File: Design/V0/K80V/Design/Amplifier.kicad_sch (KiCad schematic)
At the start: 51 parts, among them Q1 BC850, U1 AD8012, U2 AD8012, U3 LM4050AEM3-2.5+T, U4 OPA828, U5 INA828, U6 AD5752AREZ, U7 ADA4807, U8 X9118

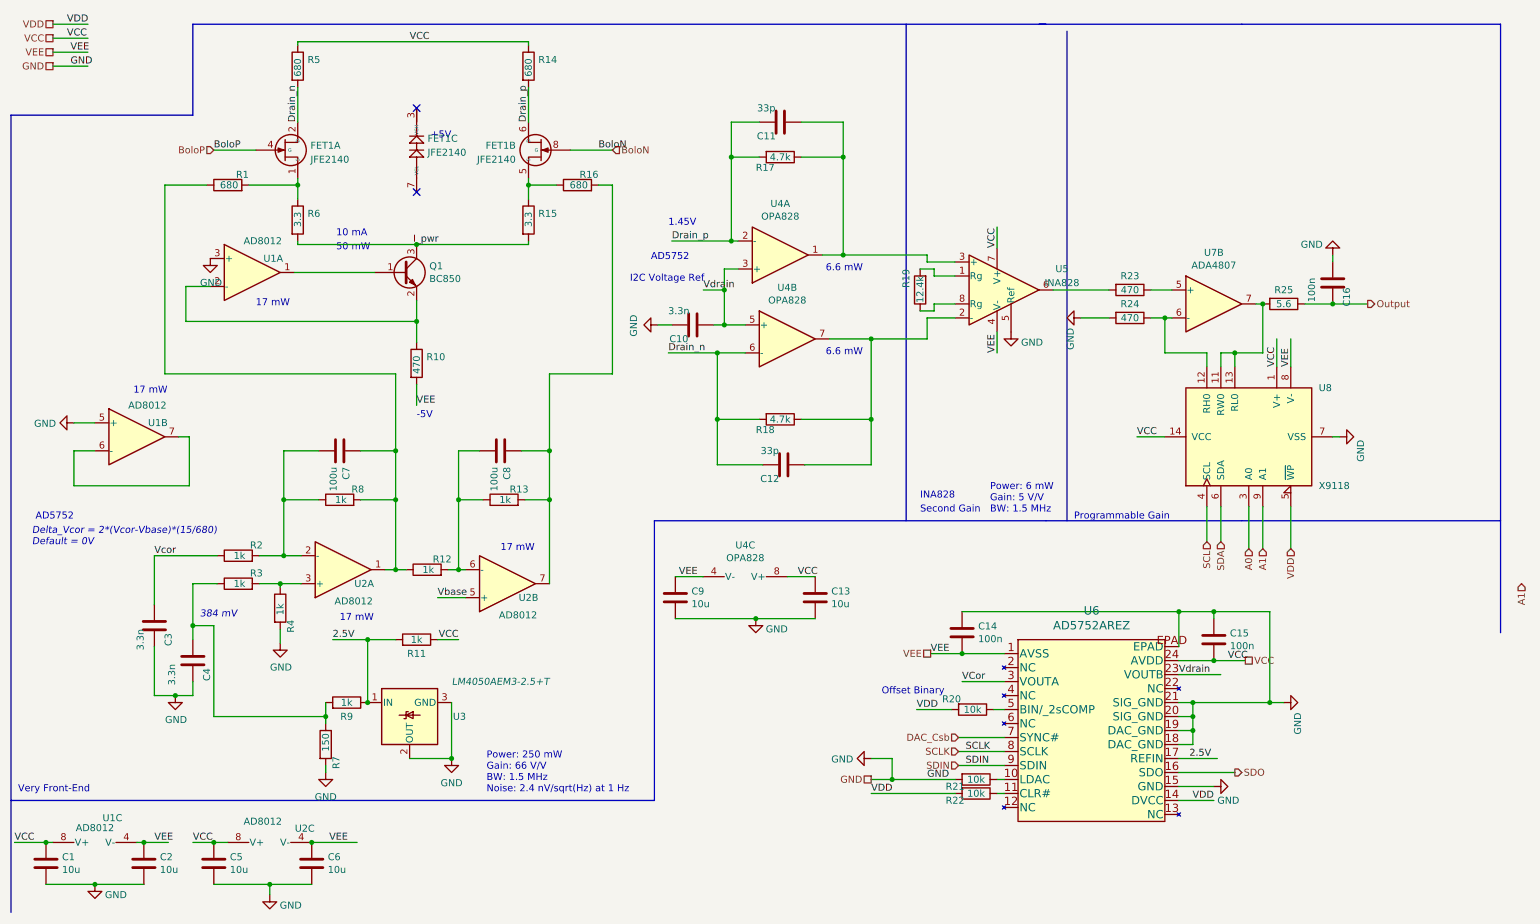
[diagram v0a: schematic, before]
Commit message: Revert "affectation des empreinte aux composants (sauf INA828)"
This reverts commit de148a86d1230cf15cf11b6507912a1ff5f95125.
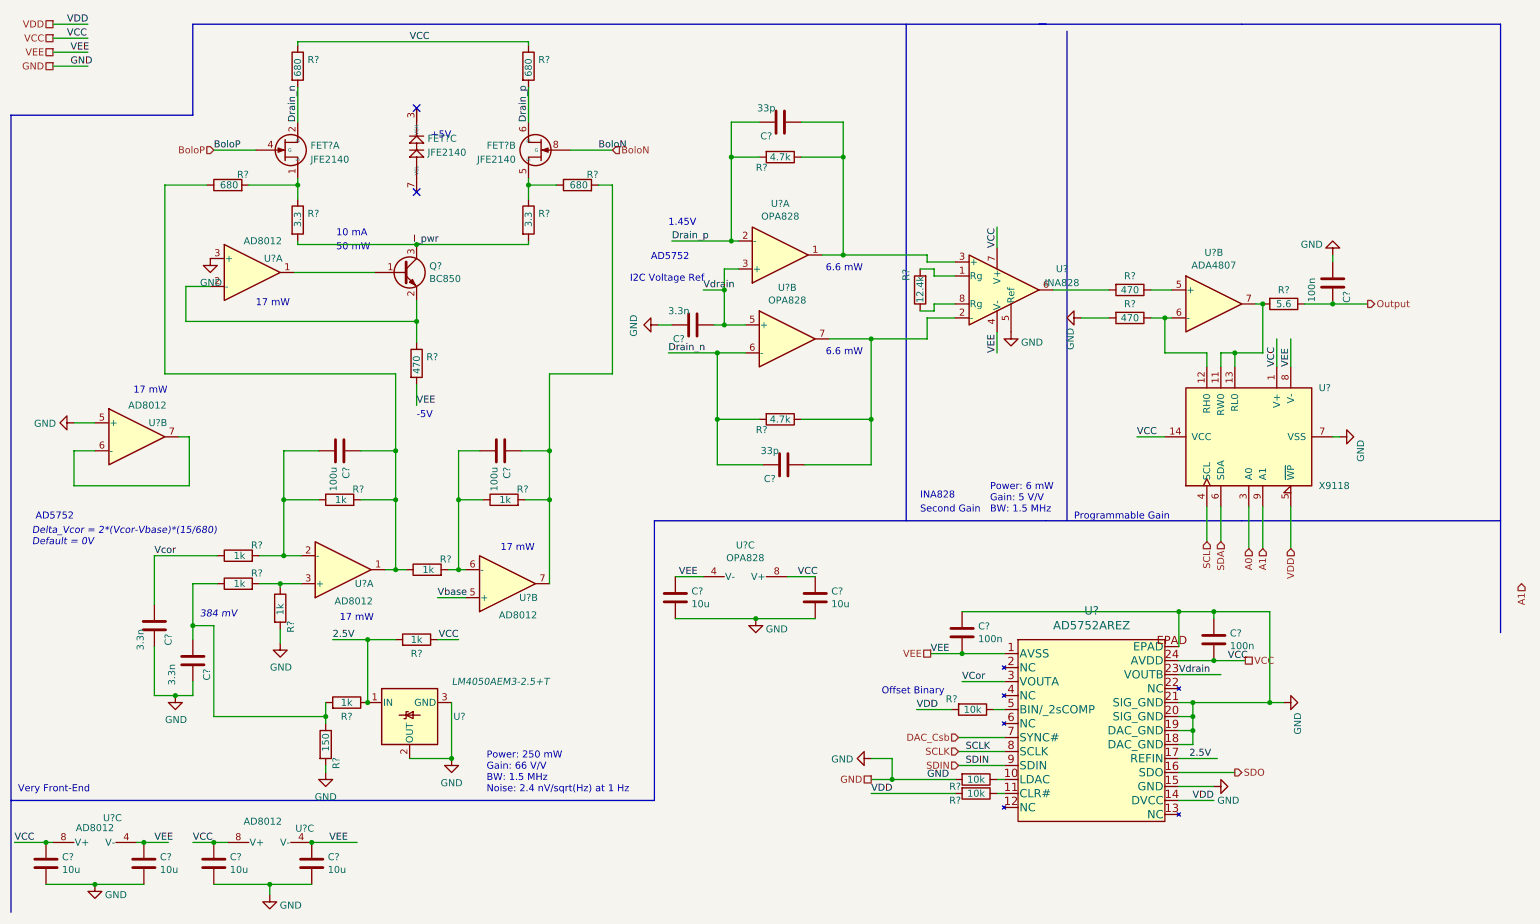
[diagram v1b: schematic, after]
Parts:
- C?: renamed from C11; footprint Capacitor_SMD:C_0805_2012Metric -> Design:C_0805_2012Metric
- C?: renamed from C1; footprint Capacitor_SMD:C_0805_2012Metric -> Design:C_0805_2012Metric
- C?: renamed from C14; footprint Capacitor_SMD:C_0805_2012Metric -> Design:C_0805_2012Metric
- C?: renamed from C13; footprint Capacitor_SMD:C_0805_2012Metric -> Design:C_0805_2012Metric
- C?: renamed from C16; footprint Capacitor_SMD:C_0805_2012Metric -> Design:C_0805_2012Metric
- C?: renamed from C9; footprint Capacitor_SMD:C_0805_2012Metric -> Design:C_0805_2012Metric
- C?: renamed from C12; footprint Capacitor_SMD:C_0805_2012Metric -> Design:C_0805_2012Metric
- C?: renamed from C8; footprint Capacitor_SMD:C_1210_3225Metric -> Design:C_1210_3225Metric
- C?: renamed from C5; footprint Capacitor_SMD:C_0805_2012Metric -> Design:C_0805_2012Metric
- C?: renamed from C3; footprint Capacitor_SMD:C_0805_2012Metric -> Design:C_0805_2012Metric
- C?: renamed from C10; footprint Capacitor_SMD:C_0805_2012Metric -> Design:C_0805_2012Metric
- C?: renamed from C7; footprint Capacitor_SMD:C_1210_3225Metric -> Design:C_1210_3225Metric
- C?: renamed from C2; footprint Capacitor_SMD:C_0805_2012Metric -> Design:C_0805_2012Metric
- C?: renamed from C15; footprint Capacitor_SMD:C_0805_2012Metric -> Design:C_0805_2012Metric
- C?: renamed from C6; footprint Capacitor_SMD:C_0805_2012Metric -> Design:C_0805_2012Metric
- C?: renamed from C4; footprint Capacitor_SMD:C_0805_2012Metric -> Design:C_0805_2012Metric
- R?: renamed from R1; footprint Resistor_SMD:R_MELF_MMB-0207 -> Design:R_MELF_MMB-0207
- R?: renamed from R17; footprint Resistor_SMD:R_MELF_MMB-0207 -> Design:R_MELF_MMB-0207
- R?: renamed from R6; footprint Resistor_SMD:R_MELF_MMB-0207 -> Design:R_MELF_MMB-0207
- R?: renamed from R16; footprint Resistor_SMD:R_MELF_MMB-0207 -> Design:R_MELF_MMB-0207
- R?: renamed from R7; footprint Resistor_SMD:R_MELF_MMB-0207 -> Design:R_MELF_MMB-0207
- R?: renamed from R18; footprint Resistor_SMD:R_MELF_MMB-0207 -> Design:R_MELF_MMB-0207
- R?: renamed from R23; footprint Resistor_SMD:R_0805_2012Metric -> Design:R_0805_2012Metric
- R?: renamed from R9; footprint Resistor_SMD:R_0805_2012Metric -> Design:R_0805_2012Metric
- R?: renamed from R2; footprint Resistor_SMD:R_MELF_MMB-0207 -> Design:R_MELF_MMB-0207
- R?: renamed from R24; footprint Resistor_SMD:R_0805_2012Metric -> Design:R_0805_2012Metric
- R?: renamed from R22; footprint Resistor_SMD:R_0805_2012Metric -> Design:R_0805_2012Metric
- R?: renamed from R4; footprint Resistor_SMD:R_MELF_MMB-0207 -> Design:R_MELF_MMB-0207
- R?: renamed from R3; footprint Resistor_SMD:R_MELF_MMB-0207 -> Design:R_MELF_MMB-0207
- R?: renamed from R13; footprint Resistor_SMD:R_MELF_MMB-0207 -> Design:R_MELF_MMB-0207
- R?: renamed from R14; footprint Resistor_SMD:R_MELF_MMB-0207 -> Design:R_MELF_MMB-0207
- R?: renamed from R5; footprint Resistor_SMD:R_MELF_MMB-0207 -> Design:R_MELF_MMB-0207
- R?: renamed from R21; footprint Resistor_SMD:R_0805_2012Metric -> Design:R_0805_2012Metric
- R?: renamed from R15; footprint Resistor_SMD:R_MELF_MMB-0207 -> Design:R_MELF_MMB-0207
- R?: renamed from R19; footprint Resistor_SMD:R_MELF_MMB-0207 -> Design:R_MELF_MMB-0207
- R?: renamed from R11; footprint Resistor_SMD:R_0805_2012Metric -> Design:R_0805_2012Metric
- R?: renamed from R20; footprint Resistor_SMD:R_0805_2012Metric -> Design:R_0805_2012Metric
- R?: renamed from R25; footprint Resistor_SMD:R_0805_2012Metric -> Design:R_0805_2012Metric
- R?: renamed from R8; footprint Resistor_SMD:R_MELF_MMB-0207 -> Design:R_MELF_MMB-0207
- R?: renamed from R10; footprint Resistor_SMD:R_MELF_MMB-0207 -> Design:R_MELF_MMB-0207
- R?: renamed from R12; footprint Resistor_SMD:R_MELF_MMB-0207 -> Design:R_MELF_MMB-0207
- U?: renamed from U7; footprint Package_SO:MSOP-8_3x3mm_P0.65mm -> Design:MSOP-8_3x3mm_P0.65mm
- U? (x3): renamed from U1; footprint Package_SO:SOIC-8_3.9x4.9mm_P1.27mm -> Design:SOIC-8_3.9x4.9mm_P1.27mm
- U? (x3): renamed from U2; footprint Package_SO:SOIC-8_3.9x4.9mm_P1.27mm -> Design:SOIC-8_3.9x4.9mm_P1.27mm
- U? (x3): renamed from U4; footprint Package_SO:SOIC-8_3.9x4.9mm_P1.27mm -> Design:SOIC-8_3.9x4.9mm_P1.27mm
- U?: renamed from U3; footprint Package_SO:TSOP-6_1.65x3.05mm_P0.95mm -> Design:SOT-23
- U?: renamed from U6; footprint baclet_composants_np:AD5752AREZ -> Design:AD5752AREZ
- U?: renamed from U8; footprint Package_SO:TSSOP-14_4.4x5mm_P0.65mm -> Design:TSSOP-14_4.4x5mm_P0.65mm
- renumbered FET1 to FET?, Q1 to Q?, U5 to U?

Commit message: Revert "Revert "affectation des empreinte aux composants (sauf INA828)""
This reverts commit 838fc88806717458eb0e77e457d551168a8dcae9.
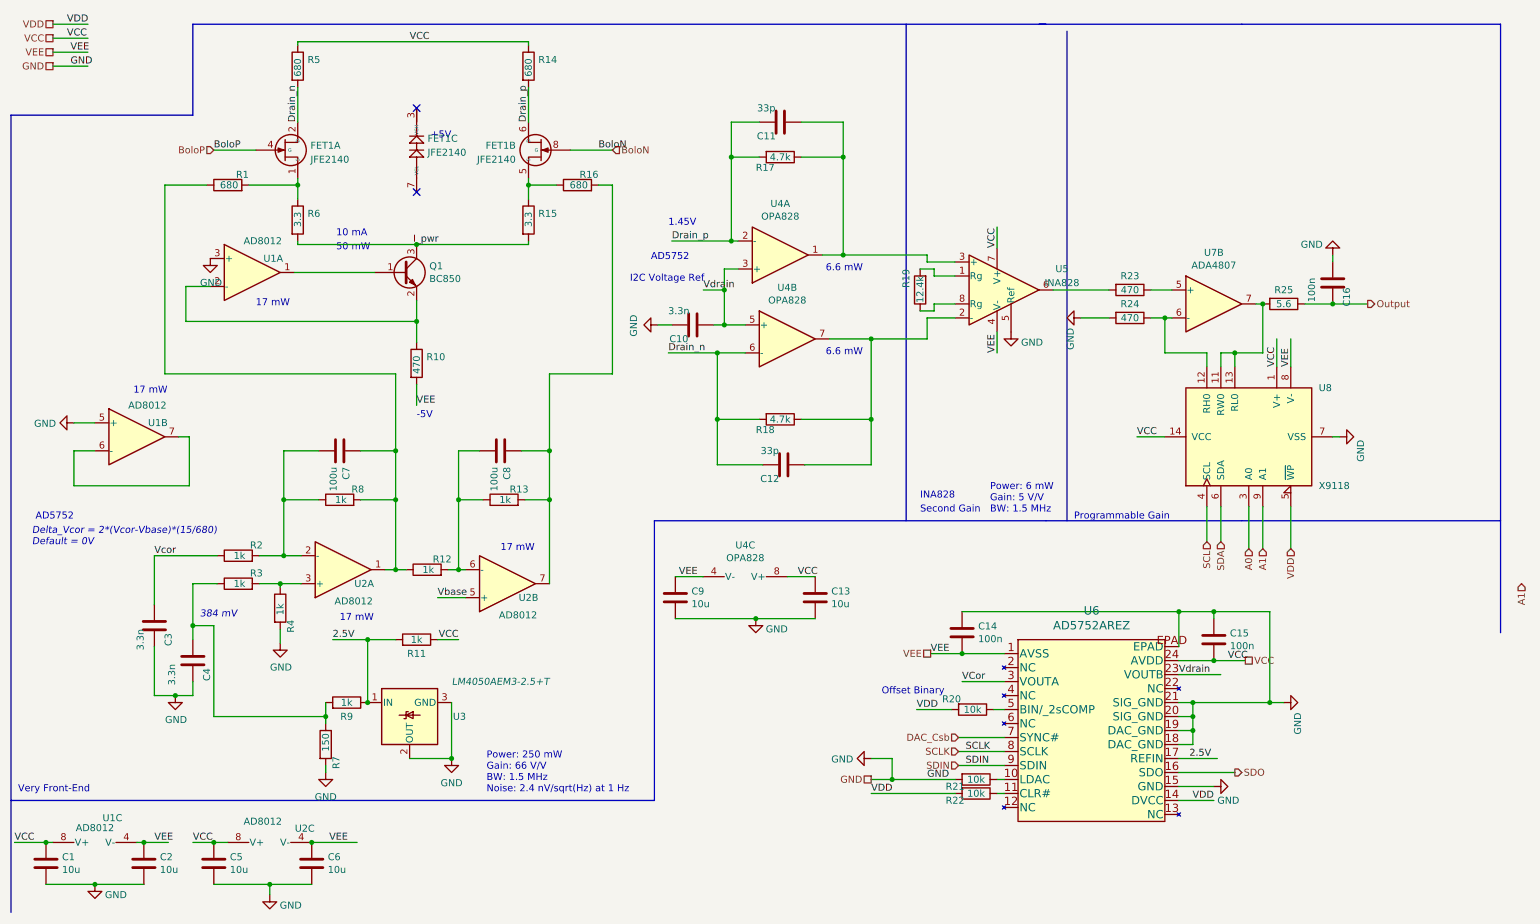
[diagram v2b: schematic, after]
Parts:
- C1, C10, C11, C12, C13, C14, C15, C16, C2, C3, C4, C5, C6, C9: renamed from C?; footprint Design:C_0805_2012Metric -> Capacitor_SMD:C_0805_2012Metric
- C7, C8: renamed from C?; footprint Design:C_1210_3225Metric -> Capacitor_SMD:C_1210_3225Metric
- R1, R10, R12, R13, R14, R15, R16, R17, R18, R19, R2, R3, R4, R5, R6, R7, R8: renamed from R?; footprint Design:R_MELF_MMB-0207 -> Resistor_SMD:R_MELF_MMB-0207
- R11, R20, R21, R22, R23, R24, R25, R9: renamed from R?; footprint Design:R_0805_2012Metric -> Resistor_SMD:R_0805_2012Metric
- U1, U2, U4: renamed from U?; footprint Design:SOIC-8_3.9x4.9mm_P1.27mm -> Package_SO:SOIC-8_3.9x4.9mm_P1.27mm
- U3: renamed from U?; footprint Design:SOT-23 -> Package_SO:TSOP-6_1.65x3.05mm_P0.95mm
- U6: renamed from U?; footprint Design:AD5752AREZ -> baclet_composants_np:AD5752AREZ
- U7: renamed from U?; footprint Design:MSOP-8_3x3mm_P0.65mm -> Package_SO:MSOP-8_3x3mm_P0.65mm
- U8: renamed from U?; footprint Design:TSSOP-14_4.4x5mm_P0.65mm -> Package_SO:TSSOP-14_4.4x5mm_P0.65mm
- gave numbers to parts that had none: 3
